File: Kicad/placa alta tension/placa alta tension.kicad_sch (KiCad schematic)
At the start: 35 parts, among them J1 Power, J2 Digital/PWM, J3 Analog, J4 Digital/PWM, J5 Screw_Terminal_01x02, J6 Screw_Terminal_01x02, J7 Screw_Terminal_01x02, Q1 BT136-600, Q2 2N7000, Q3 2N7000, Q4 BT136-600, U1 4N25, U2 MOC3023M, U3 MOC3023M

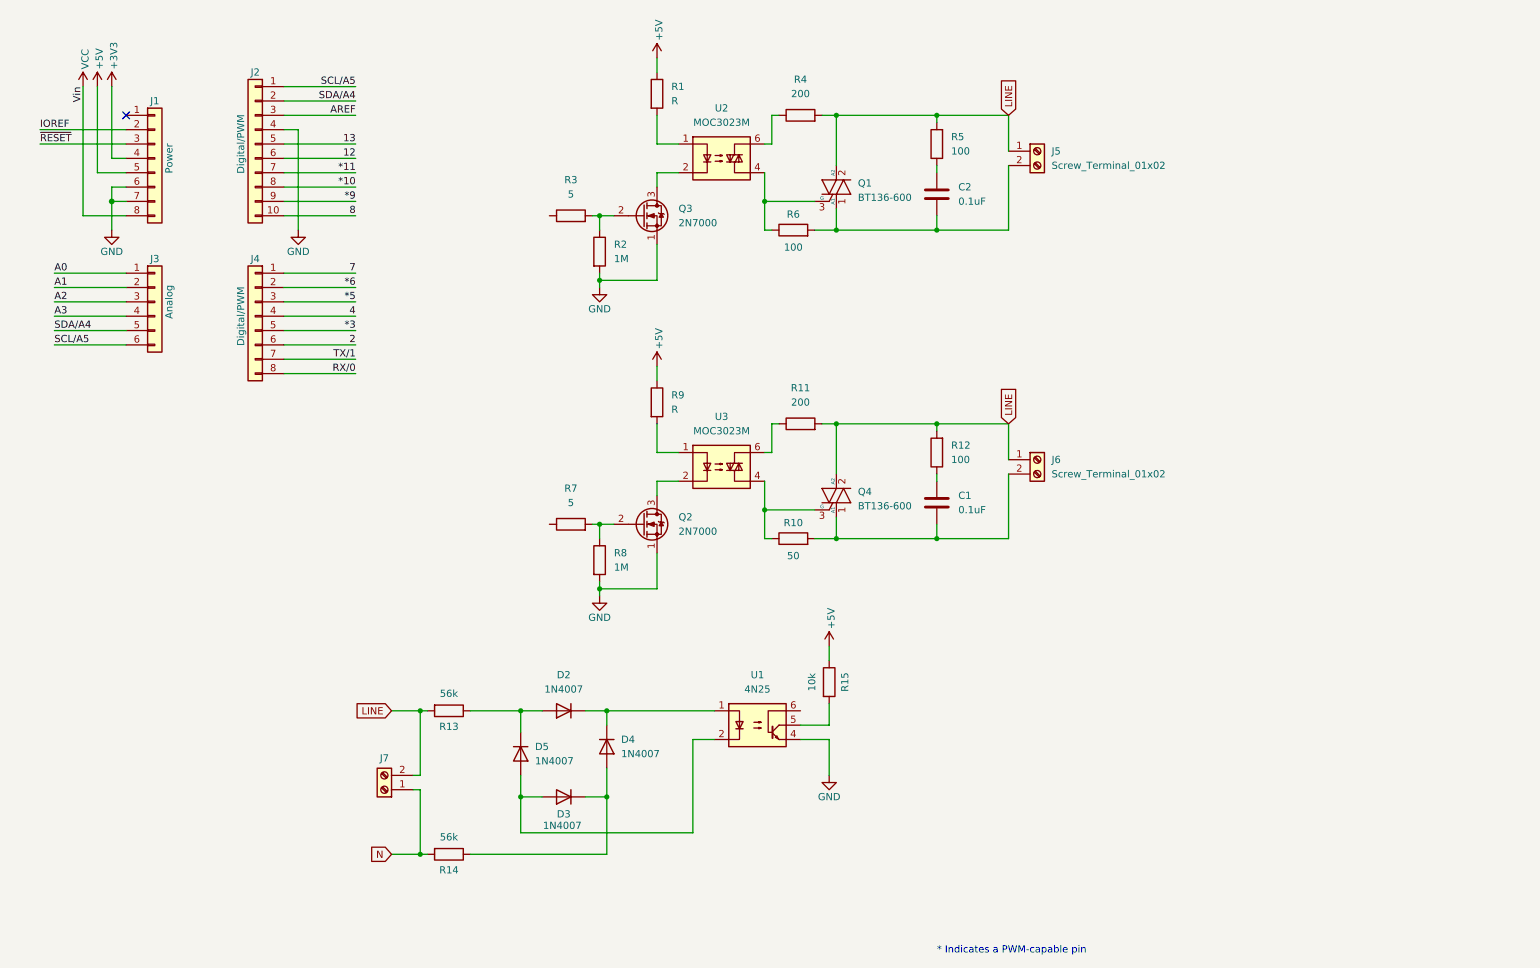
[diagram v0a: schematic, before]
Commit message: shield arrancado
Faltaría rutear y ver si podemos hacer algo para fabricarlo nosotros o si o si va a tener que ser doble faz. Sería interesante probar fabricar en china.
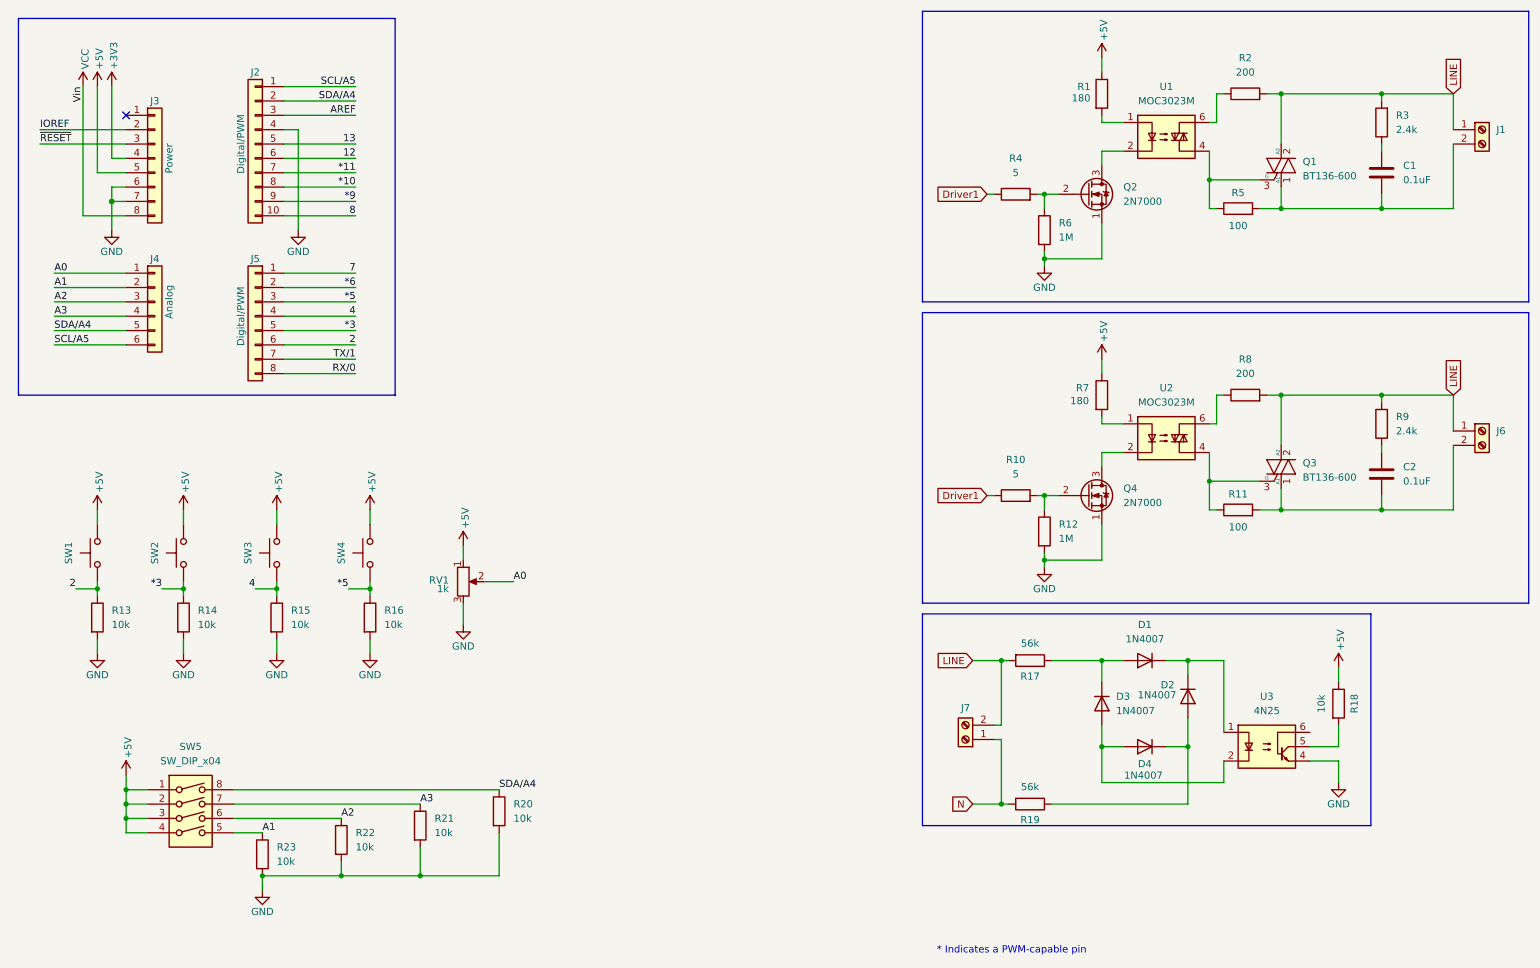
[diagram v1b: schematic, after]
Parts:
- removed C1: 0.1uF, symbol Device:C
- removed Q2: 2N7000, Package_TO_SOT_THT:TO-92_Inline, symbol Transistor_FET:2N7000
- removed Q4: BT136-600, Package_TO_SOT_THT:TO-220-3_Vertical, symbol Triac_Thyristor:BT136-600
- removed U3: MOC3023M, symbol Relay_SolidState:MOC3023M
- added C2: 0.1uF, Capacitor_THT:C_Rect_L18.0mm_W9.0mm_P15.00mm_FKS3_FKP3, symbol Device:C
- added Q3: BT136-600, Package_TO_SOT_THT:TO-220-3_Vertical, symbol Triac_Thyristor:BT136-600
- added Q4: 2N7000, Package_TO_SOT_THT:TO-92_Inline, symbol Transistor_FET:2N7000
- added R13, R14, R15, R16, R20, R21, R22, R23: 10k, Resistor_THT:R_Axial_DIN0207_L6.3mm_D2.5mm_P7.62mm_Horizontal, symbol Device:R
- added RV1: 1k, Potentiometer_THT:Potentiometer_Alps_RK163_Single_Horizontal, symbol Device:R_Potentiometer
- added SW1, SW2, SW3, SW4: SW_Push, Button_Switch_THT:SW_PUSH_6mm, symbol Switch:SW_Push
- added SW5: SW_DIP_x04, Button_Switch_THT:SW_DIP_SPSTx04_Slide_9.78x12.34mm_W7.62mm_P2.54mm, symbol Switch:SW_DIP_x04
- added U2: MOC3023M, Package_DIP:DIP-6_W7.62mm_Socket_LongPads, symbol Relay_SolidState:MOC3023M
- C1: renamed from C2; footprint (none) -> Capacitor_THT:C_Rect_L18.0mm_W9.0mm_P15.00mm_FKS3_FKP3
- J1: renamed from J5; footprint (none) -> TerminalBlock_Phoenix:TerminalBlock_Phoenix_MKDS-1,5-2-5.08_1x02_P5.08mm_Horizontal
- J6, J7: footprint (none) -> TerminalBlock_Phoenix:TerminalBlock_Phoenix_MKDS-1,5-2-5.08_1x02_P5.08mm_Horizontal
- R1: value R -> 180; footprint (none) -> Resistor_THT:R_Axial_DIN0207_L6.3mm_D2.5mm_P7.62mm_Horizontal
- R10: value 50 -> 5; footprint (none) -> Resistor_THT:R_Axial_DIN0207_L6.3mm_D2.5mm_P7.62mm_Horizontal
- R11: value 200 -> 100; footprint (none) -> Resistor_THT:R_Axial_DIN0207_L6.3mm_D2.5mm_P7.62mm_Horizontal
- R12: value 100 -> 1M; footprint (none) -> Resistor_THT:R_Axial_DIN0207_L6.3mm_D2.5mm_P7.62mm_Horizontal
- R17: renamed from R13; footprint (none) -> Resistor_THT:R_Axial_DIN0614_L14.3mm_D5.7mm_P15.24mm_Horizontal
- R18: renamed from R15; footprint (none) -> Resistor_THT:R_Axial_DIN0207_L6.3mm_D2.5mm_P7.62mm_Horizontal
- R19: renamed from R14; footprint (none) -> Resistor_THT:R_Axial_DIN0614_L14.3mm_D5.7mm_P15.24mm_Horizontal
- R2: renamed from R4; footprint (none) -> Resistor_THT:R_Axial_DIN0207_L6.3mm_D2.5mm_P7.62mm_Horizontal
- R3: renamed from R5; value 100 -> 2.4k; footprint (none) -> Resistor_THT:R_Axial_DIN0614_L14.3mm_D5.7mm_P15.24mm_Horizontal
- R4: renamed from R3; footprint (none) -> Resistor_THT:R_Axial_DIN0207_L6.3mm_D2.5mm_P7.62mm_Horizontal
- R5: renamed from R6; footprint (none) -> Resistor_THT:R_Axial_DIN0207_L6.3mm_D2.5mm_P7.62mm_Horizontal
- R6: renamed from R2; footprint (none) -> Resistor_THT:R_Axial_DIN0207_L6.3mm_D2.5mm_P7.62mm_Horizontal
- R7: value 5 -> 180; footprint (none) -> Resistor_THT:R_Axial_DIN0207_L6.3mm_D2.5mm_P7.62mm_Horizontal
- R8: value 1M -> 200; footprint (none) -> Resistor_THT:R_Axial_DIN0207_L6.3mm_D2.5mm_P7.62mm_Horizontal
- R9: value R -> 2.4k; footprint (none) -> Resistor_THT:R_Axial_DIN0614_L14.3mm_D5.7mm_P15.24mm_Horizontal
- U1: renamed from U2; footprint (none) -> Package_DIP:DIP-6_W7.62mm_Socket_LongPads
- renumbered D2 to D1, D4 to D2, D5 to D3, D3 to D4, J1 to J3, J3 to J4, J4 to J5, Q3 to Q2, U1 to U3
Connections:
- net *3: now also R14.1, SW2.1
- net *5: now also R16.1, SW4.1
- net +5V: now also R7.1, RV1.1, SW1.2, SW2.2, SW3.2, SW4.2, SW5.1, SW5.2, SW5.3, SW5.4; no longer R9.1
- net 2: now also R13.1, SW1.1
- net 4: now also R15.1, SW3.1
- net A0: now also RV1.2
- net A1: now also R23.1, SW5.5
- net A2: now also R22.1, SW5.6
- net A3: now also R21.1, SW5.7
- net GND: now also R12.2, Q4.1 (S), R13.2, R14.2, R15.2, R16.2, R20.2, R21.2, R22.2, R23.2, RV1.3; no longer R8.2
- net LINE: now also R8.2, R9.2, Q3.2 (A2); no longer R11.2, R12.2
- net SDA/A4: now also R20.1, SW5.8
- net at R12.1: now also R10.2, Q4.2 (G)
- net at J6.2 (Pin_2): now also R11.2, C2.2, Q3.1 (A1); no longer R10.2
- net Driver1: now reaches R4.1
- net Driver1: now also R10.1
- net at R7.2: now also U2.1; no longer R8.1
- net at R11.1: now also Q3.3 (G), U2.4
- new net: C2.1, R9.1
- new net: Q4.3 (D), U2.2
- new net: R8.1, U2.6
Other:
- moved on the sheet: C1, D1, D2, D3, D4, J1, J7, Q1, Q2, R1, R17, R18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

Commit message: placa 220
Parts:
- removed J2: Digital/PWM, Connector_PinSocket_2.54mm:PinSocket_1x10_P2.54mm_Vertical, symbol Connector_Generic:Conn_01x10
- removed J3: Power, Connector_PinSocket_2.54mm:PinSocket_1x08_P2.54mm_Vertical, symbol Connector_Generic:Conn_01x08
- removed J4: Analog, Connector_PinSocket_2.54mm:PinSocket_1x06_P2.54mm_Vertical, symbol Connector_Generic:Conn_01x06
- removed J5: Digital/PWM, Connector_PinSocket_2.54mm:PinSocket_1x08_P2.54mm_Vertical, symbol Connector_Generic:Conn_01x08
- removed R13, R14, R15, R16, R20, R21, R22, R23: 10k, Resistor_THT:R_Axial_DIN0207_L6.3mm_D2.5mm_P7.62mm_Horizontal, symbol Device:R
- removed RV1: 1k, Potentiometer_THT:Potentiometer_Alps_RK163_Single_Horizontal, symbol Device:R_Potentiometer
- removed SW1, SW2, SW3, SW4: SW_Push, Button_Switch_THT:SW_PUSH_6mm, symbol Switch:SW_Push
- removed SW5: SW_DIP_x04, Button_Switch_THT:SW_DIP_SPSTx04_Slide_9.78x12.34mm_W7.62mm_P2.54mm, symbol Switch:SW_DIP_x04
- added J9: Conn_01x05_Pin, Connector_PinHeader_2.54mm:PinHeader_1x05_P2.54mm_Vertical, symbol Connector:Conn_01x05_Pin
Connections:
- net +5V: now also J9.5 (Pin_5)
- net GND: now also J9.4 (Pin_4)
- net LINE: no longer J1.1 (Pin_1), J6.1 (Pin_1), Q1.2 (A2), Q3.2 (A2), R2.2, R3.2, R8.2, R9.2
- net ZCD: now reaches R18.2, U3.5
- net ZCD: now also J9.3 (Pin_3)
- net Driver1 renamed DIMM1
- net DIMM1: now also J9.1 (Pin_1); no longer R4.1
- new net DIMM2: J9.2 (Pin_2), R4.1
- new net LINE1: J6.1 (Pin_1), Q3.2 (A2), R8.2, R9.2
- new net LINE2: J1.1 (Pin_1), Q1.2 (A2), R2.2, R3.2
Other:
- moved on the sheet: R18

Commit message: placa
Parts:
- removed J7: Screw_Terminal_01x02, TerminalBlock_Phoenix:TerminalBlock_Phoenix_MKDS-1,5-2-5.08_1x02_P5.08mm_Horizontal, symbol Connector:Screw_Terminal_01x02
- removed J9: Conn_01x05_Pin, Connector_PinHeader_2.54mm:PinHeader_1x05_P2.54mm_Vertical, symbol Connector:Conn_01x05_Pin
- added J1: Conn_01x05_Socket, Connector_PinHeader_2.54mm:PinHeader_1x05_P2.54mm_Horizontal, symbol Connector:Conn_01x05_Socket
- added J3: Screw_Terminal_01x02, TerminalBlock_Phoenix:TerminalBlock_Phoenix_MKDS-1,5-2-5.08_1x02_P5.08mm_Horizontal, symbol Connector:Screw_Terminal_01x02
- U2: renamed from U3; footprint Package_DIP:DIP-6_W7.62mm -> Package_DIP:DIP-6_W7.62mm_Socket_LongPads
- renumbered J1 to J2, J6 to J4, R17 to R1, R7 to R10, R8 to R11, R9 to R12, R10 to R13, R11 to R14, R12 to R15, R1 to R2, R2 to R3, R18 to R4, R3 to R5, R4 to R6, R19 to R7, R5 to R8, R6 to R9, U2 to U3
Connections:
- net LINE1 is gone; now on net DIMMING_LINE: J4.1 (Pin_1), Q3.2 (A2), R11.2, R12.2
- net +5V: now also J1.2 (Pin_2)
- net GND: now also J1.1 (Pin_1)
- net N: now also J3.1 (Pin_1)
- net ZCD: now also J1.3 (Pin_3)
- net DIMM1 renamed FAN
- net FAN: now also J1.4 (Pin_4)
- net DIMM2 renamed LIGHT
- net LIGHT: now also J1.5 (Pin_5)
- net LINE renamed DIMMING_LINE
- net DIMMING_LINE: now also J3.2 (Pin_2)
- net LINE2 renamed LIGHT_LINE
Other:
- moved on the sheet: C1, C2, D1, D2, D3, D4, J2, J4, Q1, Q2, Q3, Q4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

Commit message: simuklaciones ltspice y ajustes antes de comprar comps
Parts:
- removed Q1, Q3: BT136-600, Package_TO_SOT_THT:TO-220-3_Vertical, symbol Triac_Thyristor:BT136-600
- added D5, D6: Generic_Triac_A1A2G, Package_TO_SOT_THT:TO-220-3_Vertical, symbol Triac_Thyristor:Generic_Triac_A1A2G
- R1, R7: value 56k -> 18k
- R11, R3: value 200 -> 220
- R14, R8: value 100 -> 220
- R4: value 10k -> 1k
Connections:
- net DIMMING_LINE: now also D6.2 (A2)
- net LIGHT_LINE: now also D5.2 (A2)
- net at C1.2, J2.2 (Pin_2), R8.2: now also D5.1 (A1)
- net at R14.1, U3.4: now also D6.3 (G)
- net at C2.2, J4.2 (Pin_2), R14.2: now also D6.1 (A1)
- net at R8.1, U1.4: now also D5.3 (G)
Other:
- note added: "BTA16-800 BTA12-800 BTA06-600C"

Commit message: consulta Fede
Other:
- moved on the sheet: J1
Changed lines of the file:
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@@
 	(rectangle
 		(start 124.46 14.605)
-		(end 218.44 52.07)
+		(end 218.44 53.34)
 		(stroke
 			(width 0)
@@
 	)
 	(rectangle
-		(start 222.25 22.225)
-		(end 245.11 43.18)
+		(start 219.71 14.605)
+		(end 242.57 35.56)
 		(stroke
 			(width 0)
@@
 	(wire
 		(pts
-			(xy 236.22 34.29) (xy 229.87 34.29)
+			(xy 233.68 26.67) (xy 227.33 26.67)
 		)
 		(stroke
@@
 	(wire
 		(pts
-			(xy 237.49 39.37) (xy 229.87 39.37)
+			(xy 234.95 31.75) (xy 227.33 31.75)
 		)
 		(stroke
@@
 	(wire
 		(pts
-			(xy 229.87 36.83) (xy 233.68 36.83)
+			(xy 227.33 29.21) (xy 231.14 29.21)
 		)
 		(stroke
@@
 	(wire
 		(pts
-			(xy 236.22 31.75) (xy 229.87 31.75)
+			(xy 233.68 24.13) (xy 227.33 24.13)
 		)
 		(stroke
@@
 	(wire
 		(pts
-			(xy 236.22 29.21) (xy 229.87 29.21)
+			(xy 233.68 21.59) (xy 227.33 21.59)
 		)
 		(stroke
@@
 	)
 	(label "LIGHT"
-		(at 236.22 29.21 180)
+		(at 233.68 21.59 180)
 		(effects
 			(font
@@
 	)
 	(label "ZCD"
-		(at 236.22 34.29 0)
+		(at 233.68 26.67 0)
 		(effects
 			(font
@@
 	)
 	(label "FAN"
-		(at 236.22 31.75 180)
+		(at 233.68 24.13 180)
 		(effects
 			(font
@@
 	(symbol
 		(lib_id "Connector:Conn_01x05_Socket")
-		(at 224.79 34.29 180)
+		(at 222.25 26.67 180)
 		(unit 1)
 		(exclude_from_sim no)
@@
 		(dnp no)
 		(property "Reference" "J1"
-			(at 226.314 26.162 0)
+			(at 223.774 18.542 0)
 			(effects
 				(font
@@
 		)
 		(property "Value" "Conn_01x05_Socket"
-			(at 225.425 26.67 0)
+			(at 222.885 19.05 0)
 			(effects
 				(font
@@
 		)
 		(property "Footprint" "Connector_PinHeader_2.54mm:PinHeader_1x05_P2.54mm_Horizontal"
-			(at 224.79 34.29 0)
+			(at 222.25 26.67 0)
 			(effects
 				(font
@@
 		)
 		(property "Datasheet" "~"
-			(at 224.79 34.29 0)
+			(at 222.25 26.67 0)
 			(effects
 				(font
@@
 		)
 		(property "Description" "Generic connector, single row, 01x05, script generated"
-			(at 224.79 34.29 0)
+			(at 222.25 26.67 0)
 			(effects
 				(font
@@
 	(symbol
 		(lib_id "power:GND")
-		(at 237.49 39.37 90)
+		(at 234.95 31.75 90)
 		(mirror x)
 		(unit 1)
@@
 		(dnp no)
 		(property "Reference" "#PWR04"
-			(at 243.84 39.37 0)
+			(at 241.3 31.75 0)
 			(effects
 				(font
@@
 		)
 		(property "Value" "GND"
-			(at 241.3 39.37 0)
+			(at 238.76 31.75 0)
 			(effects
 				(font
@@
 		)
 		(property "Footprint" ""
-			(at 237.49 39.37 0)
+			(at 234.95 31.75 0)
 			(effects
 				(font
@@
 		)
 		(property "Datasheet" ""
-			(at 237.49 39.37 0)
+			(at 234.95 31.75 0)
 			(effects
 				(font
@@
 		)
 		(property "Description" "Power symbol creates a global label with name \"GND\" , ground"
-			(at 237.49 39.37 0)
+			(at 234.95 31.75 0)
 			(effects
 				(font
@@
 	(symbol
 		(lib_id "power:+5V")
-		(at 233.68 36.83 270)
+		(at 231.14 29.21 270)
 		(mirror x)
 		(unit 1)
@@
 		(dnp no)
 		(property "Reference" "#PWR03"
-			(at 229.87 36.83 0)
+			(at 227.33 29.21 0)
 			(effects
 				(font
@@
 		)
 		(property "Value" "+5V"
-			(at 236.728 36.4744 90)
+			(at 234.188 28.8544 90)
 			(effects
 				(font
@@
 		)
 		(property "Footprint" ""
-			(at 233.68 36.83 0)
+			(at 231.14 29.21 0)
 			(effects
 				(font
@@
 		)
 		(property "Datasheet" ""
-			(at 233.68 36.83 0)
+			(at 231.14 29.21 0)
 			(effects
 				(font
@@
 		)
 		(property "Description" "Power symbol creates a global label with name \"+5V\""
-			(at 233.68 36.83 0)
+			(at 231.14 29.21 0)
 			(effects
 				(font

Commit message: placa v2
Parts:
- added F1, F2, F3: Fuse, Fuse:Fuseholder_Clip-5x20mm_Bel_FC-203-22_Lateral_P17.80x5.00mm_D1.17mm_Horizontal, symbol Device:Fuse
- added R6: 2k, Resistor_THT:R_Axial_DIN0411_L9.9mm_D3.6mm_P12.70mm_Horizontal, symbol Device:R
- added RV1, RV2, RV3: Varistor, Varistor:RV_Disc_D15.5mm_W4.2mm_P7.5mm, symbol Device:Varistor
- added U3: 74HC14, Package_DIP:DIP-14_W7.62mm_Socket_LongPads, symbol 74xx:74HC14
- Q1: renamed from Q2; footprint Package_TO_SOT_THT:TO-92_Inline -> Package_TO_SOT_THT:TO-92_Wide
- Q2: renamed from Q4; footprint Package_TO_SOT_THT:TO-92_Inline -> Package_TO_SOT_THT:TO-92_Wide
- R1: value 18k -> 10k
- R8: renamed from R7; value 18k -> 10k
- renumbered D5 to D4, D4 to D5, J2 to J1, J3 to J2, J4 to J3, J1 to J4, R9 to R10, R10 to R11, R11 to R12, R12 to R13, R13 to R14, R14 to R15, R15 to R16, R6 to R7, R8 to R9, U3 to U4
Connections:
- net +5V: now also U3.14 (VCC)
- net DIMMING_LINE: now also F3.2; no longer D6.2 (A2), J2.2 (Pin_2), R1.2, R12.2, R13.2
- net FAN: now also J4.5 (Pin_5), U3.9; no longer J4.4 (Pin_4), R14.1
- net GND: now also U3.1, U3.3, U3.5, U3.7 (GND)
- net LIGHT: now also J4.4 (Pin_4), U3.11; no longer J4.5 (Pin_5), R7.1
- net LIGHT_LINE: now also F2.2; no longer D4.2 (A2), R3.2, R5.2
- net N: now also F1.1, RV1.2; no longer J2.1 (Pin_1)
- net ZCD: now also U3.12; no longer R4.2, U2.5
- net HV11: now reaches C1.2, D4.1 (A1), J1.2 (Pin_2), R9.2
- net HV11: now also RV2.2
- net at C2.2, D6.1 (A1), J3.2 (Pin_2)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: now also RV3.2
- net HV9: now reaches D2.2 (A), D5.1 (K), R8.1
- net at D3.2 (A), D5.2 (A): now also R6.2; no longer U2.2
- new net: J2.2 (Pin_2), R1.2, RV1.1
- new net: D6.2 (A2), F3.1, R12.2, R13.2, RV3.1
- new net: R7.1, U3.10
- new net: R6.1, U2.2
- new net: R4.2, U2.5, U3.13
- new net: D4.2 (A2), F2.1, R3.2, R5.2, RV2.1
- new net: F1.2, J2.1 (Pin_1)
- new net: R14.1, U3.8
- no-connect marks 1 -> 4
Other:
- note removed: "BTA16-800 BTA12-800 BTA06-600C"
- moved on the sheet: C1, C2, D1, D2, D3, D4, D5, D6, J1, J2, J3, J4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

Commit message: placa terminada
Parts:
- added TP10, TP11, TP12, TP13, TP16, TP3, TP4, TP5, TP6, TP7, TP8, TP9: TestPoint, Connector_PinHeader_2.54mm:PinHeader_1x01_P2.54mm_Vertical, symbol Connector:TestPoint
- D4, D6: value Generic_Triac_A1A2G -> BTA06-600C
- R13, R5: value 2.4k -> 1k
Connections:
- net GND: now also TP16.1
- net HV11: now also TP10.1
- net at D6.2 (A2), F3.1, R12.2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: now also TP3.1
- net at D6.3 (G), R15.1, U4.4: now also TP5.1
- net at C2.2, D6.1 (A1), J3.2 (Pin_2)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: now also TP4.1
- net at D4.3 (G), R9.1, U1.4: now also TP8.1
- net at R3.1, U1.6: now also TP7.1
- net at R6.1, U2.2: now also TP12.1
- net at R4.2, U2.5, U3.13: now also TP13.1
- net at D4.2 (A2), F2.1, R3.2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: now also TP9.1
- net at R12.1, U4.6: now also TP6.1
- net at D1.1 (K), D2.1 (K), U2.1: now also TP11.1
